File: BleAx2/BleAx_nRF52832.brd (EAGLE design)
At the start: 55.7 x 22.9 mm, 41 parts, among them CN1 6p-2.54, J5 MICROUSB, U1 NRF52832, U2 TLV1117, X1 32MHz, X2 32.768kHz

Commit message: power ldo
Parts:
- removed U2: TLV1117, Nordic_misc:SOT220P700-4_N
- added U4: MIC5225-3.3, microbuilder:SOT23-5
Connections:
- net GND: now also U4.2; no longer U2.1
- net VDD_P3V3: now also U4.5; no longer U2.2, U2.4
- net VDD_P5V0: now also U4.1, U4.3; no longer U2.3
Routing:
- net VDD_P5V0: track 40.5 -> 16.9 mm, vias 1 -> 0
- net VDD_P3V3: track 62.4 -> 51.8 mm
- net P0.07: track 3.05 -> 0.99 mm, vias 1 -> 0
- net P0.06: track 2.96 -> 0.99 mm, vias 1 -> 0
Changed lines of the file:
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@@
 <grid distance="0.01" unitdist="mm" unit="mm" style="lines" multiple="1" display="yes" altdistance="0.05" altunitdist="mm" altunit="mm"/>
 <layers>
-<layer number="1" name="Top" color="4" fill="1" visible="yes" active="yes"/>
+<layer number="1" name="Top" color="4" fill="1" visible="no" active="yes"/>
 <layer number="2" name="Route2" color="1" fill="3" visible="no" active="no"/>
 <layer number="3" name="Route3" color="4" fill="3" visible="no" active="no"/>
@@
 <layer number="14" name="Route14" color="1" fill="6" visible="no" active="no"/>
 <layer number="15" name="Route15" color="4" fill="6" visible="no" active="no"/>
-<layer number="16" name="Bottom" color="1" fill="1" visible="no" active="yes"/>
+<layer number="16" name="Bottom" color="1" fill="1" visible="yes" active="yes"/>
 <layer number="17" name="Pads" color="2" fill="1" visible="yes" active="yes"/>
 <layer number="18" name="Vias" color="2" fill="1" visible="yes" active="yes"/>
@@
 <attribute name="VALUE" x="43.44" y="8.85" size="1.27" layer="27"/>
 </element>
-<element name="U2" library="Nordic_misc" package="SOT220P700-4_N" value="TLV1117" x="24.9" y="11.4" smashed="yes" rot="MR0">
-<attribute name="NAME" x="24.9" y="11.4" size="1" layer="26" rot="MR0" align="center"/>
-<attribute name="VALUE" x="27.44" y="6.32" size="1.27" layer="28" rot="MR0"/>
-</element>
 <element name="L3" library="Nordic_misc" package="RESC0402_N" value="15nH" x="32.54" y="17.9" smashed="yes">
 <attribute name="NAME" x="32.04" y="17.6" size="0.6" layer="25"/>
@@
 </element>
 <element name="C13" library="Nordic_misc" package="RESC0402_N" value="100nF" x="-7.37" y="-7.37"/>
+<element name="U4" library="microbuilder" package="SOT23-5" value="MIC5225-3.3" x="24.36" y="6.48" rot="MR180"/>
 </elements>
 <signals>
@@
 <contactref element="X1" pad="4"/>
 <contactref element="X1" pad="2"/>
-<contactref element="U2" pad="1"/>
 <contactref element="C1" pad="2"/>
 <contactref element="C2" pad="2"/>
@@
 <contactref element="CN1" pad="2"/>
 <contactref element="C13" pad="2"/>
+<contactref element="U4" pad="2"/>
 <wire x1="45.14" y1="16.05" x2="46.04" y2="16" width="0" layer="19" extent="1-1"/>
 <wire x1="43.69" y1="14.7" x2="43.865" y2="16.025" width="0" layer="19" extent="1-1"/>
@@
 <wire x1="32.19" y1="14.85" x2="32.19" y2="13.8" width="0" layer="19" extent="1-1"/>
 <wire x1="30.1" y1="13" x2="32.19" y2="13.8" width="0" layer="19" extent="1-16"/>
-<wire x1="27.8" y1="13.7" x2="30.1" y2="13" width="0" layer="19" extent="16-16"/>
-<wire x1="27.94" y1="15" x2="27.8" y2="13.7" width="0" layer="19" extent="16-16"/>
+<wire x1="27.94" y1="15" x2="30.1" y2="13" width="0" layer="19" extent="16-16"/>
 <wire x1="27.04" y1="14.85" x2="27.94" y2="15" width="0" layer="19" extent="1-1"/>
 <wire x1="27.94" y1="17.4" x2="27.94" y2="15" width="0" layer="19" extent="1-1"/>
@@
 <wire x1="26.8" y1="5.9" x2="26.53" y2="1.76" width="0" layer="19" extent="1-16"/>
 <wire x1="27.05" y1="7.2" x2="26.8" y2="5.9" width="0" layer="19" extent="16-16"/>
+<wire x1="24.36" y1="7.7801" x2="26.53" y2="1.76" width="0" layer="19" extent="1-1"/>
 <wire x1="43.3" y1="3.68" x2="39.14" y2="9.6" width="0" layer="19" extent="1-1"/>
 <wire x1="4.3" y1="16" x2="15.475" y2="15" width="0" layer="19" extent="1-1"/>
@@
 <signal name="P0.06">
 <contactref element="R11" pad="1"/>
-<via x="18.3" y="18.4" extent="1-16" drill="0.4"/>
-<wire x1="18.3" y1="18.4" x2="18.3" y2="19.8" width="0.2" layer="16"/>
 <wire x1="18.3" y1="18.4" x2="19.15" y2="18.4" width="0.2" layer="1"/>
 <wire x1="19.15" y1="18.4" x2="19.25" y2="18.5" width="0.2" layer="1" curve="90"/>
-<wire x1="18.3" y1="19.8" x2="17.9" y2="20.2" width="0.2" layer="16"/>
 </signal>
 <signal name="P0.07">
 <contactref element="R10" pad="1"/>
-<via x="15.1" y="18.4" extent="1-16" drill="0.4"/>
 <wire x1="15.1" y1="18.4" x2="15.95" y2="18.4" width="0.2" layer="1"/>
 <wire x1="15.95" y1="18.4" x2="16.05" y2="18.5" width="0.2" layer="1" curve="90"/>
-<wire x1="15.1" y1="20.46" x2="15.1" y2="18.4" width="0.2" layer="16"/>
 </signal>
 <signal name="P0.08">
@@
 </signal>
 <signal name="VDD_P5V0">
-<contactref element="U2" pad="3"/>
 <contactref element="C16" pad="1"/>
 <contactref element="C17" pad="1"/>
-<wire x1="27.8" y1="9.1" x2="28.15" y2="8.75" width="0.6" layer="16" curve="-90"/>
-<wire x1="28.15" y1="8.75" x2="28.15" y2="7.2" width="0.6" layer="16"/>
 <wire x1="28.15" y1="7.2" x2="28.15" y2="6.15" width="0.6" layer="16"/>
 <wire x1="28.15" y1="6.15" x2="28.4" y2="5.9" width="0.6" layer="16" curve="90"/>
@@
 <wire x1="8.7" y1="16.3" x2="12" y2="18.6" width="0.3048" layer="1" curve="114.99034"/>
 <wire x1="12" y1="18.6" x2="12" y2="18.7" width="0.3048" layer="1" curve="-4.740947"/>
-<via x="12" y="18.7" extent="1-16" drill="0.6"/>
-<wire x1="12" y1="18.7" x2="12.170709375" y2="18.629290625" width="0.3048" layer="16" curve="-44.999476"/>
-<wire x1="12.170709375" y1="18.629290625" x2="16" y2="14.8" width="0.3048" layer="16"/>
-<wire x1="16" y1="14.8" x2="16" y2="12.0142125" width="0.3048" layer="16"/>
-<wire x1="16" y1="12.0142125" x2="16.29289375" y2="11.30710625" width="0.3048" layer="16" curve="45"/>
-<wire x1="16.29289375" y1="11.30710625" x2="17.9" y2="9.7" width="0.3048" layer="16"/>
-<wire x1="17.9" y1="9.7" x2="18.070709375" y2="9.629290625" width="0.3048" layer="16" curve="-44.999476"/>
-<wire x1="18.070709375" y1="9.629290625" x2="18.5" y2="9.2" width="0.3048" layer="16"/>
-<wire x1="18.5" y1="9.2" x2="27.558578125" y2="9.2" width="0.3048" layer="16"/>
-<wire x1="27.558578125" y1="9.2" x2="27.8" y2="9.1" width="0.3048" layer="16" curve="-45"/>
 <wire x1="6.3" y1="17.3" x2="6.3" y2="18.0857875" width="0.3048" layer="1"/>
 <wire x1="6.3" y1="18.0857875" x2="6.00710625" y2="18.79289375" width="0.3048" layer="1" curve="45"/>
@@
 <wire x1="1.39289375" y1="17.10710625" x2="1.5" y2="17" width="0.3048" layer="1"/>
 <wire x1="6.00710625" y1="18.79289375" x2="5.6" y2="19.2" width="0.3048" layer="1"/>
+<contactref element="U4" pad="3"/>
+<contactref element="U4" pad="1"/>
+<wire x1="25.31" y1="7.7801" x2="28.15" y2="7.2" width="0" layer="19" extent="16-16"/>
+<wire x1="23.41" y1="7.7801" x2="25.31" y2="7.7801" width="0" layer="19" extent="16-16"/>
+<wire x1="12" y1="18.6" x2="23.41" y2="7.7801" width="0" layer="19" extent="1-16"/>
 </signal>
 <signal name="VCC_P5V0_USB">
@@
 <contactref element="C8" pad="1"/>
 <contactref element="C9" pad="1"/>
-<contactref element="U2" pad="2"/>
-<contactref element="U2" pad="4"/>
 <contactref element="C18" pad="1"/>
 <contactref element="C19" pad="1"/>
@@
 <wire x1="34.4" y1="7.85" x2="34.1" y2="7.55" width="0.6" layer="16"/>
 <wire x1="34.4" y1="14.4" x2="34.4" y2="11.4" width="0.6" layer="16"/>
-<wire x1="27.8" y1="11.4" x2="30.1" y2="11.4" width="0.6" layer="16"/>
-<wire x1="19.5" y1="11.4" x2="22" y2="11.4" width="0.6" layer="16"/>
-<wire x1="22" y1="11.4" x2="27.8" y2="11.4" width="0.6" layer="16"/>
 <wire x1="30.1" y1="11.3" x2="30.1" y2="11.4" width="0.6" layer="16"/>
 <wire x1="30.1" y1="11.4" x2="34.3" y2="11.4" width="0.6" layer="16"/>
@@
 <contactref element="U3" pad="1"/>
 <contactref element="C13" pad="1"/>
-<wire x1="23.96" y1="3.09" x2="26.53" y2="3.76" width="0" layer="19" extent="1-1"/>
-<wire x1="21.8" y1="7.1" x2="23.96" y2="3.09" width="0" layer="19" extent="1-1"/>
+<contactref element="U4" pad="5"/>
+<wire x1="22.9" y1="10.7" x2="30.1" y2="11.4" width="0" layer="19" extent="1-16"/>
+<wire x1="23.96" y1="3.09" x2="21.8" y2="7.1" width="0" layer="19" extent="1-1"/>
+<wire x1="26.53" y1="3.76" x2="23.96" y2="3.09" width="0" layer="19" extent="1-1"/>
+<wire x1="23.41" y1="5.1799" x2="23.96" y2="3.09" width="0" layer="19" extent="1-1"/>
 <wire x1="-7.92" y1="-7.37" x2="14.3" y2="10.15" width="0" layer="19" extent="1-1"/>
 </signal>

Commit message: batt source
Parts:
- removed D1: LED, Nordic_misc:DIOC0603_N
- removed R12: 0R, Nordic_misc:RESC0402_N
- removed R9: 330R, Nordic_misc:RESC0402_N
- added J1: 2.0MM-90D, Seeed-OPL-Connector:H2-2.0-90D
- added R1: 2K, Nordic_misc:RESC0402_N
- added U2: MCP73832T-2ACI/OT-SOT23-5, Seeed-OPL-ic:SOT-23-5
- moved C13 23.4 mm to (9.00, 9.32)
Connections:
- removed net P0.06: R11.1
- removed net P0.07: R10.1
- removed net VDD_LED: D1.2, R9.2
- removed net VDD_P5V0: C16.1, C17.1, D1.1, R12.2, U4.1, U4.3
- new net N$1: R1.1, U2.5
- new net N$10: R11.1, U2.1
- new net VDD_BATT: C16.1, C17.1, J1.+, U2.3, U4.1, U4.3
- net GND: now also J1.-, R1.2, U2.2; no longer R9.1
- net VCC_P5V0_USB: now also D3.2, U2.4; no longer R12.1
- net VDD_P3V3: no longer D3.2
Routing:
- net VDD_P5V0: track 16.9 -> 0.00 mm
- net VDD_P3V3: track 51.8 -> 44.2 mm
- net VCC_P5V0_USB: track 5.48 -> 0.00 mm
- net N$9: track 3.54 -> 0.00 mm
- net VDD_BATT: track 0.00 -> 1.40 mm
- net VDD_LED: track 1.30 -> 0.00 mm
- net P0.07: track 0.99 -> 0.00 mm
- net P0.06: track 0.99 -> 0.00 mm
- net GND: vias 15 -> 10

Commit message: evolve
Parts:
- added U$1: 1,1/0,6, wirepad:1,1/0,6
- moved R1 15.7 mm to (5.36, 3.32)
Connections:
- new net LIS_CS: U1.11, U3.8
- new net LIS_INT1: U$1.P$1, U1.12, U3.11
- new net MISO_01: U1.10, U3.7
- new net MOSI_01: U1.9, U3.6
- new net SCK_01: U1.8, U3.4
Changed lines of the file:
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@@
 <setting verticaltext="up"/>
 </settings>
-<grid distance="0.01" unitdist="mm" unit="mm" style="lines" multiple="1" display="yes" altdistance="0.05" altunitdist="mm" altunit="mm"/>
+<grid distance="0.1" unitdist="mm" unit="mm" style="lines" multiple="1" display="yes" altdistance="0.01" altunitdist="mm" altunit="mm"/>
 <layers>
 <layer number="1" name="Top" color="4" fill="1" visible="yes" active="yes"/>
@@
 <attribute name="MPN" value="MCP73832T-2ACI/OT" x="10.06" y="3.27" size="1.778" layer="27" display="off"/>
 </element>
-<element name="R1" library="Nordic_misc" package="RESC0402_N" value="2K" x="-6.11" y="-7.37"/>
+<element name="R1" library="Nordic_misc" package="RESC0402_N" value="2K" x="5.36" y="3.32"/>
 <element name="J1" library="Seeed-OPL-Connector" package="H2-2.0-90D" value="2.0MM-90D" x="8.66" y="15.43" rot="R180"/>
+<element name="U$1" library="wirepad" package="1,1/0,6" value="1,1/0,6" x="30.68" y="6.07"/>
 </elements>
 <signals>
@@
 <wire x1="43.3" y1="3.68" x2="39.14" y2="9.6" width="0" layer="19" extent="1-1"/>
 <wire x1="10.06" y1="1.9699" x2="9.55" y2="9.32" width="0" layer="19" extent="1-1"/>
-<wire x1="-5.56" y1="-7.37" x2="10.06" y2="1.9699" width="0" layer="19" extent="1-1"/>
+<wire x1="5.91" y1="3.32" x2="10.06" y2="1.9699" width="0" layer="19" extent="1-1"/>
 </signal>
 <signal name="DEC1">
@@
 <wire x1="18.2" y1="10.7" x2="18.5" y2="10.4" width="0.2" layer="1"/>
 <wire x1="18.5" y1="10.4" x2="18.5" y2="8.2" width="0.2" layer="1"/>
+<contactref element="U4" pad="5"/>
 <contactref element="C6" pad="1"/>
+<contactref element="C13" pad="1"/>
 <contactref element="U3" pad="1"/>
-<contactref element="C13" pad="1"/>
-<contactref element="U4" pad="5"/>
 <wire x1="26.53" y1="3.76" x2="30.1" y2="11.3" width="0" layer="19" extent="1-16"/>
 <wire x1="23.96" y1="3.09" x2="26.53" y2="3.76" width="0" layer="19" extent="1-1"/>
@@
 <contactref element="U2" pad="5"/>
 <contactref element="R1" pad="1"/>
-<wire x1="-6.66" y1="-7.37" x2="9.11" y2="4.5701" width="0" layer="19" extent="1-1"/>
+<wire x1="4.81" y1="3.32" x2="9.11" y2="4.5701" width="0" layer="19" extent="1-1"/>
 </signal>
 <signal name="N$10">
@@
 <wire x1="9.11" y1="1.9699" x2="19.25" y2="18.5" width="0" layer="19" extent="1-1"/>
 </signal>
+<signal name="MISO_01">
+<contactref element="U3" pad="7"/>
+<contactref element="U1" pad="10"/>
+<wire x1="27.98" y1="1.31" x2="34.34" y2="10" width="0" layer="19" extent="1-1"/>
+</signal>
+<signal name="SCK_01">
+<contactref element="U3" pad="4"/>
+<contactref element="U1" pad="8"/>
+<wire x1="26.53" y1="2.26" x2="34.34" y2="10.8" width="0" layer="19" extent="1-1"/>
+</signal>
+<signal name="MOSI_01">
+<contactref element="U3" pad="6"/>
+<contactref element="U1" pad="9"/>
+<wire x1="27.48" y1="1.31" x2="34.34" y2="10.4" width="0" layer="19" extent="1-1"/>
+</signal>
+<signal name="LIS_CS">
+<contactref element="U3" pad="8"/>
+<contactref element="U1" pad="11"/>
+<wire x1="28.48" y1="1.31" x2="34.34" y2="9.6" width="0" layer="19" extent="1-1"/>
+</signal>
+<signal name="LIS_INT1">
+<contactref element="U3" pad="11"/>
+<contactref element="U$1" pad="P$1"/>
+<contactref element="U1" pad="12"/>
+<wire x1="30.68" y1="6.07" x2="34.34" y2="9.2" width="0" layer="19" extent="1-1"/>
+<wire x1="29.43" y1="2.76" x2="30.68" y2="6.07" width="0" layer="19" extent="1-1"/>
+</signal>
 </signals>

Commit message: sst26
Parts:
- added U$2: SST26VF, sst26:SOIJ8
- R1: value 2K -> 3K
- R10, R11: value 330R -> 1k
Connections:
- new net MISO_02: U$2.P$2, U1.15
- new net MOSI_02: U$2.P$5, U1.16
- new net SCK_02: U$2.P$6, U1.17
- new net SST26_CE: U$2.P$1, U1.14
- net GND: now also U$2.P$4
- net VCC: no longer CN1.1
- net VDD_P3V3: now also CN1.1, U$2.P$3, U$2.P$7, U$2.P$8
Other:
- board text removed: "00"
- board text removed: "01"
- board text removed: "02"
- board text removed: "03"
- board text removed: "04"
- board text removed: "05"
- board text removed: "06"
- board text removed: "07"
- board text removed: "08"
- board text removed: "09"
- board text removed: "10"
- board text removed: "11"
- board text removed: "12"
- board text removed: "13"
- board text removed: "14"
- board text removed: "15"
- board text removed: "16"
- board text removed: "17"
- board text removed: "18"
- board text removed: "19"
- board text removed: "20"
- board text removed: "21"
- board text removed: "22"
- board text removed: "23"
- board text removed: "24"
- board text removed: "25"
- board text removed: "26"
- board text removed: "27"
- board text removed: "28"
- board text removed: "29"
- board text removed: "30"
- board text removed: "31"
- board text removed: "3V3"
- board text removed: "4"
- board text removed: "5"
- board text removed: "5V0"
- board text removed: "BTN1"
- board text removed: "CR1632"
- board text removed: "GND"
- board text removed: "J5"
- board text removed: "J6"
- board text removed: "J7"
- board text removed: "J8"
- board text removed: "LED1"
- board text removed: "LED2"
- board text removed: "NFCT"
- board text removed: "PWR"
- board text removed: "RESET"
- board text removed: "nRF52832"
- board text removed: "nRF52832_MCU_Board"

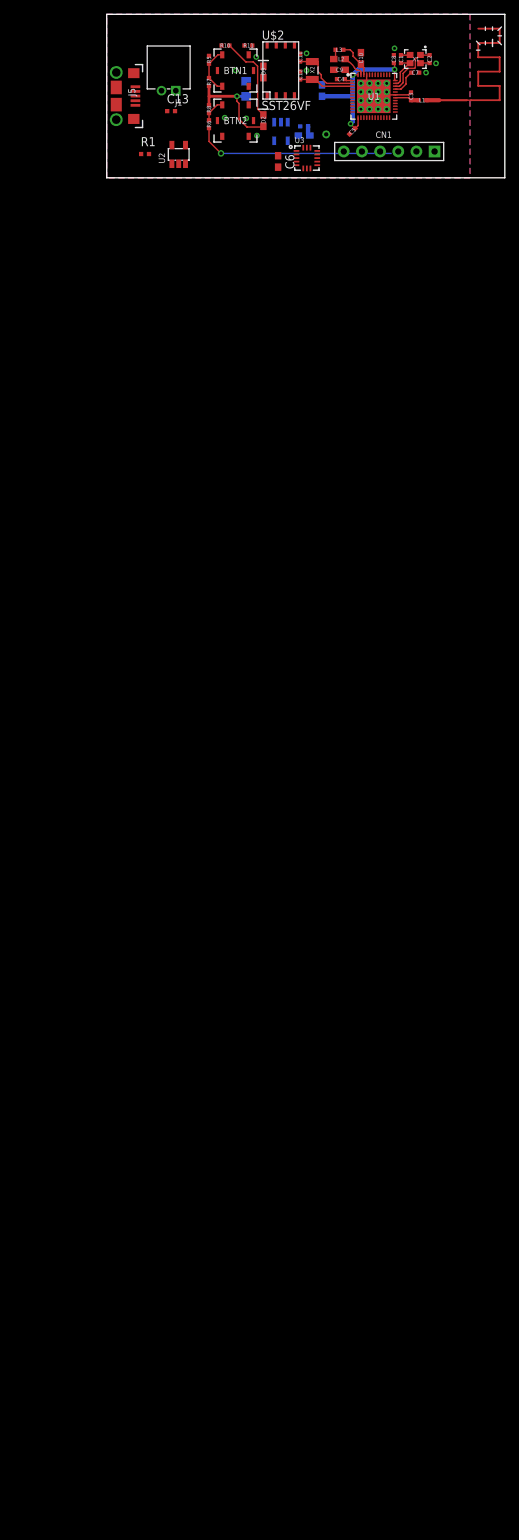
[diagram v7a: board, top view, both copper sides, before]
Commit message: evolving pads added
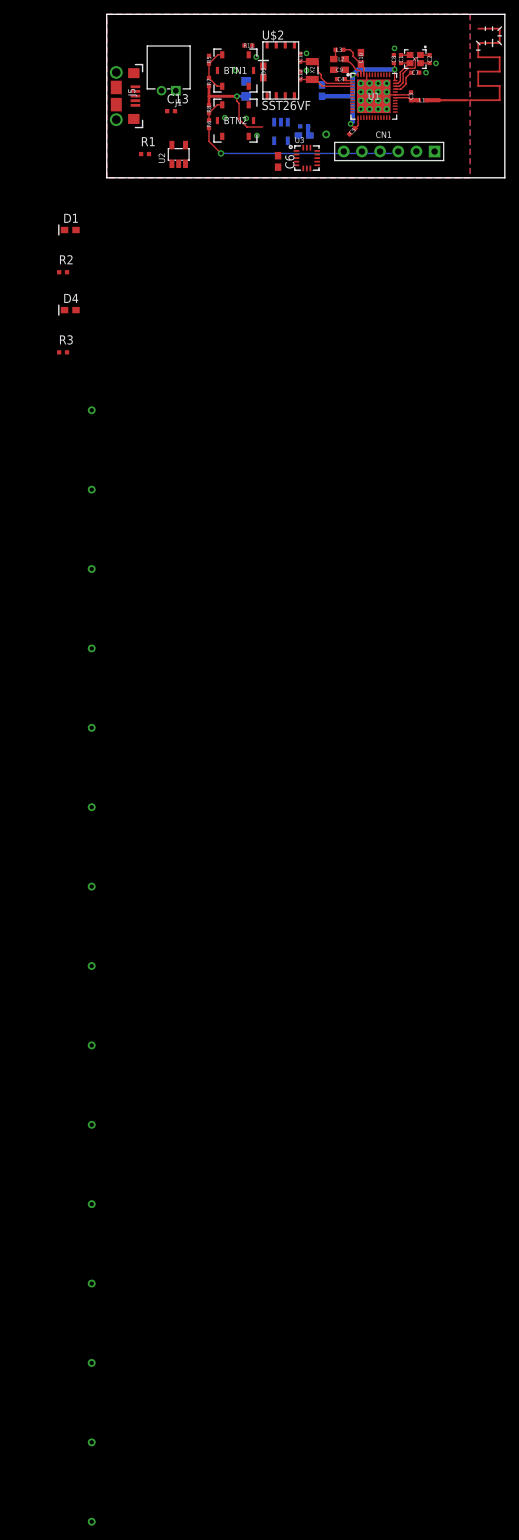
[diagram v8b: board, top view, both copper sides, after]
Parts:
- removed D2: LED, Nordic_misc:DIOC0603_N
- removed R10: 1k, Nordic_misc:RESC0402_N
- added D1, D4: LED, Nordic_misc:DIOC0603_N
- added R2, R3: 1k, Nordic_misc:RESC0402_N
- added U$10, U$11, U$12, U$13, U$14, U$15, U$16, U$17, U$3, U$4, U$5, U$6, U$7, U$8, U$9: 1,1/0,6, wirepad:1,1/0,6
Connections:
- removed net P0.08: R5.1
- new net BTTN_01: R5.1, U1.43
- new net LED_01: R2.1, U1.42
- new net LED_02: R3.1, U1.41
- new net N$11: D1.1, R2.2
- new net N$12: D4.1, R3.2
- new net N$13: U$12.P$1, U1.19
- new net N$14: U$13.P$1, U1.20
- net LIS_CS: now also U$3.P$1
- net MISO_01: now also U$4.P$1
- net MISO_02: now also U$14.P$1
- net MOSI_01: now also U$5.P$1
- net MOSI_02: now also U$16.P$1
- net N$8: now also U$11.P$1, U1.18; no longer D2.1, R10.2
- net SCK_01: now also U$6.P$1
- net SCK_02: now also U$17.P$1
- net SST26_CE: now also U$15.P$1
- net VDD_P3V3: now also D1.2, D4.2; no longer D2.2
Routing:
- net N$8: track 12.3 -> 0.00 mm
